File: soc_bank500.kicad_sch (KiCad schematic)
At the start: 38 parts, among them SW4 DTS04GE, U21 XC7Z030_FBG676, U23 S25FL128SAGMFI000, U24 TCA6408ARGTR

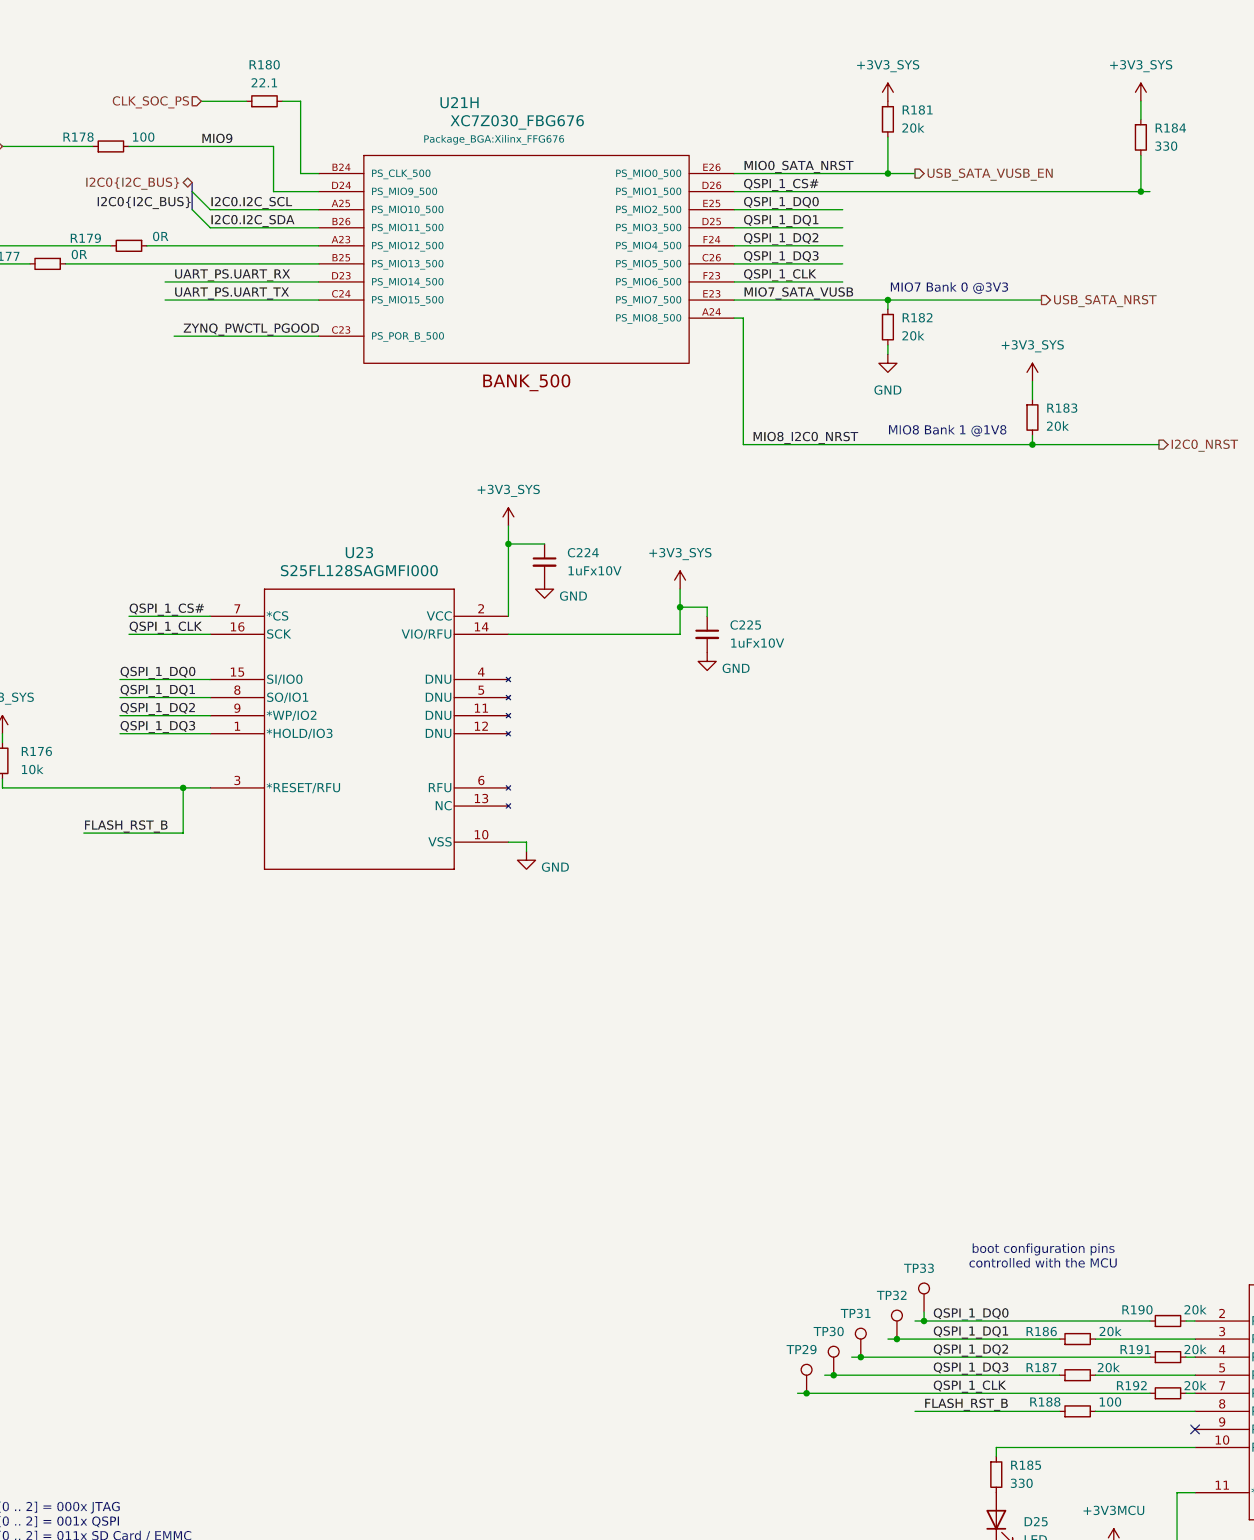
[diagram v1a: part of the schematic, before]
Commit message: schema: JTAG connector & resistors, rev change
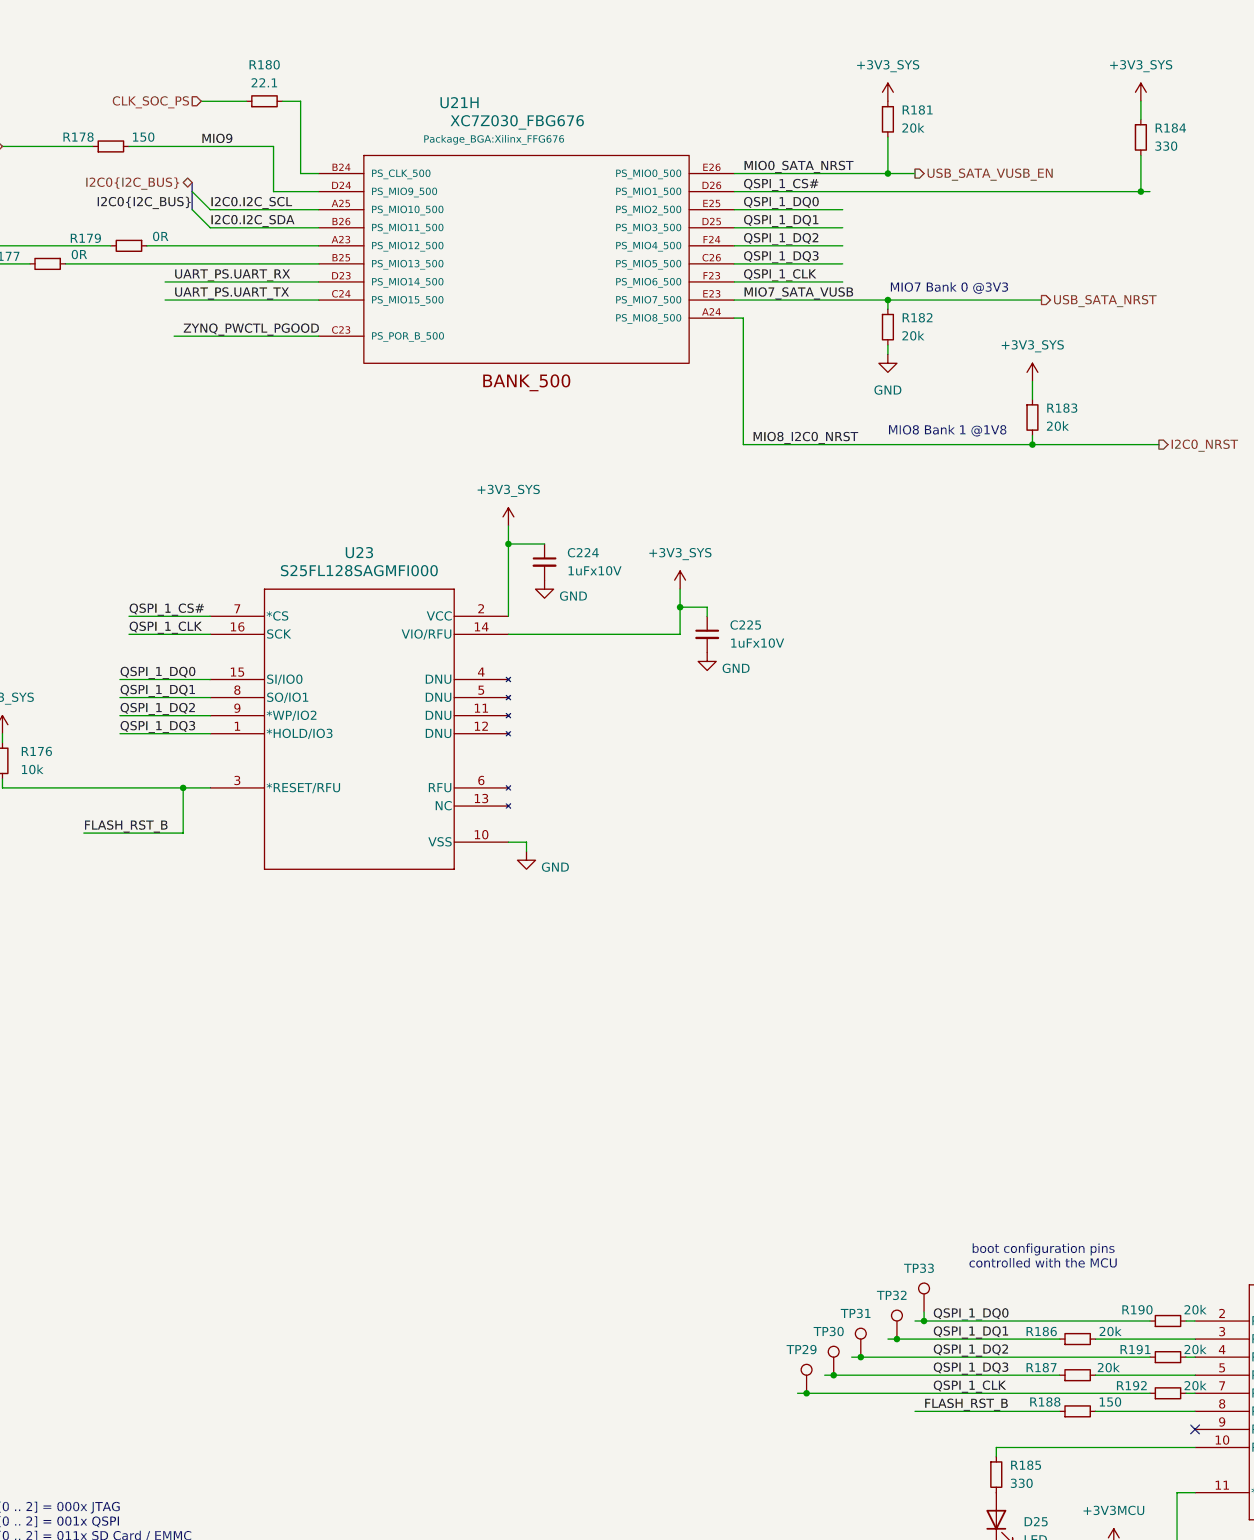
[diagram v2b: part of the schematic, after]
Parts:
- R178, R188: value 100 -> 150; JLCPCB Part # C153111 -> C25082; Part RM04FTN1000 -> 0402WGF1500TCE
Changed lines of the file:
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@@
 		(title "NASR-M")
 		(date "2025-10-22")
-		(rev "D 0.9.5")
+		(rev "D 0.9.8")
 		(company "electrodyssey.net")
 		(comment 1 "Bank 500; QSPI / Boot mode switches / POR")
@@
 		(comment 3 "Author: Nazim Aghabayov")
 		(comment 4 "SYZYGY Carrier Mainboard")
-		(comment 5 "rel: Fletched Bustard")
+		(comment 5 "rel: Wild Goose")
 	)
 	(bus_alias "I2C_BUS"
@@
 			)
 		)
-		(property "Value" "100"
+		(property "Value" "150"
 			(at 111.252 33.02 90)
 			(effects
@@
 			)
 		)
-		(property "JLCPCB Part #" "C153111"
+		(property "JLCPCB Part #" "C25082"
 			(at 106.68 34.29 0)
 			(effects
@@
 			)
 		)
-		(property "Part" "RM04FTN1000"
+		(property "Part" "0402WGF1500TCE"
 			(at 106.68 34.29 90)
 			(effects
@@
 			)
 		)
-		(property "Value" "100"
+		(property "Value" "150"
 			(at 247.142 210.82 90)
 			(effects
@@
 			)
 		)
-		(property "JLCPCB Part #" "C153111"
+		(property "JLCPCB Part #" "C25082"
 			(at 242.57 212.09 0)
 			(effects
@@
 			)
 		)
-		(property "Part" "RM04FTN1000"
+		(property "Part" "0402WGF1500TCE"
 			(at 242.57 212.09 90)
 			(effects

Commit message: schema: set R184 / MIO1 to 20k
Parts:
- R184: value 330 -> 20k; JLCPCB Part # C25104 -> C705678; Part 0402WGF3300TCE -> RT0402DRE0720KL
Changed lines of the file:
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@@
 			)
 		)
-		(property "Value" "330"
+		(property "Value" "20k"
 			(at 253.365 34.29 0)
 			(effects
@@
 			)
 		)
-		(property "Description" ""
+		(property "Description" "-55℃~+155℃ 20kΩ 50V 62.5mW Thin Film Resistor ±0.5% ±50ppm/℃ 0402 Chip Resistor - Surface Mount ROHS"
 			(at 251.46 33.02 0)
 			(effects
@@
 			)
 		)
-		(property "JLCPCB Part #" "C25104"
+		(property "JLCPCB Part #" "C705678"
 			(at 251.46 33.02 0)
 			(effects
@@
 			)
 		)
-		(property "Part" "0402WGF3300TCE"
+		(property "Part" "RT0402DRE0720KL"
 			(at 251.46 33.02 0)
 			(effects
